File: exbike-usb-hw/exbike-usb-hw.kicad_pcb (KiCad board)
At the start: 2 copper layers, 18.3 x 51.3 mm, 18 parts, among them J1 ICSP, J2 USB_B, J3 AudioJack3_SwitchTR, U1 ATtiny24A-SS, U2 AMS1117-3.3, Y1 12 MHz

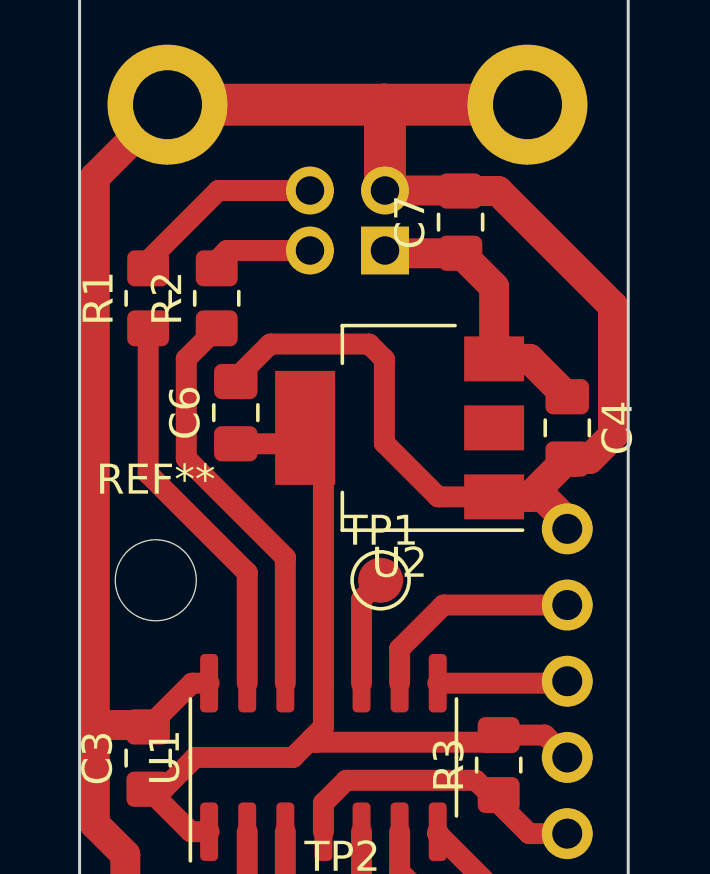
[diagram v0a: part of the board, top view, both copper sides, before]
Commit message: Add d- pullup:
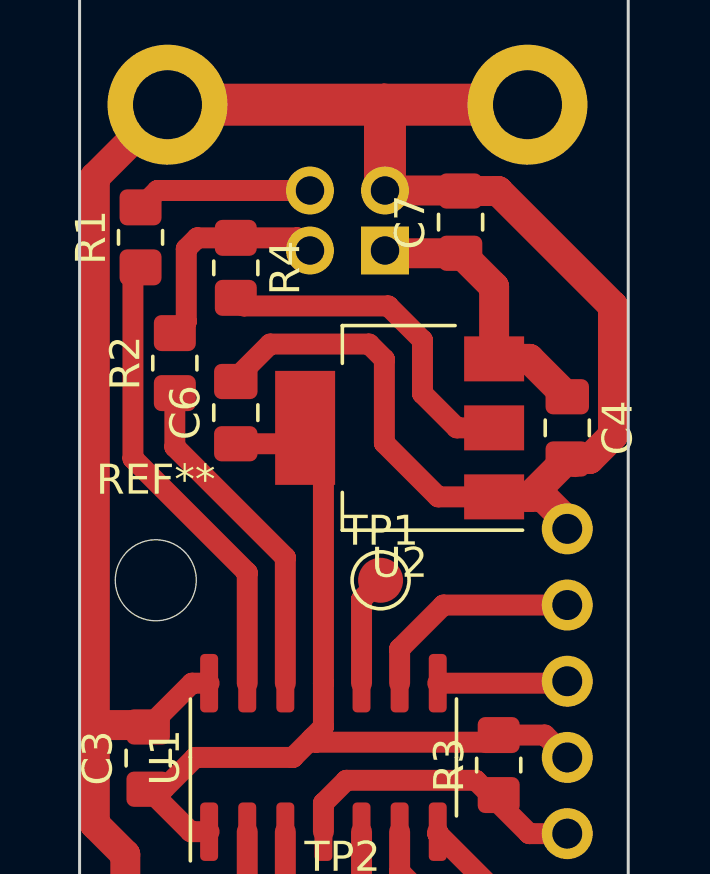
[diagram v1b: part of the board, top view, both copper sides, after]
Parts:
- added R4: 1.5k, Resistor_SMD:R_0805_2012Metric_Pad1.20x1.40mm_HandSolder, F.Cu at (66.4, 35.1)
- moved R2 2.57 mm to (64.4, 38.2)
- moved R1 2.05 mm to (63.2, 34.0)
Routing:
- net +3V3: track 31.3 -> 42.8 mm
- net D-: track 3.61 -> 7.42 mm
- net Net-(U1-PA1): track 13.6 -> 11.2 mm
- net Net-(U1-AREF/PA0): track 13.2 -> 15.5 mm
- net D+: track 6.72 -> 5.88 mm
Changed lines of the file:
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@@
+    )
+  )
+  (footprint "Resistor_SMD:R_0805_2012Metric_Pad1.20x1.40mm_HandSolder" (layer "F.Cu")
+    (at 66.421 35.052 -90)
+    (descr "Resistor SMD 0805 (2012 Metric), square (rectangular) end terminal, IPC_7351 nominal with elongated pad for handsoldering. (Body size source: IPC-SM-782 page 72, https://www.pcb-3d.com/wordpress/wp-content/uploads/ipc-sm-782a_amendment_1_and_2.pdf), generated with kicad-footprint-generator")
+    (tags "resistor handsolder")
+    (property "Sheetfile" "exbike-usb-hw.kicad_sch")
+    (property "Sheetname" "")
+    (property "ki_description" "Resistor")
+    (property "ki_keywords" "R res resistor")
+    (attr smd)
+    (fp_text reference "R4" (at 0 -1.65 90) (layer "F.SilkS")
+        (effects (font (size 1 1) (thickness 0.15)))
+    )
+    (fp_text value "1.5k" (at 0 1.65 90) (layer "F.Fab")
+        (effects (font (size 1 1) (thickness 0.15)))
+    )
+    (fp_text user "${REFERENCE}" (at 0 0 90) (layer "F.Fab")
+        (effects (font (size 0.5 0.5) (thickness 0.08)))
+    )
+    (fp_line (start -0.227064 -0.735) (end 0.227064 -0.735)
+      (stroke (width 0.12) (type solid)) (layer "F.SilkS"))
+    (fp_line (start -0.227064 0.735) (end 0.227064 0.735)
+      (stroke (width 0.12) (type solid)) (layer "F.SilkS"))
+    (fp_line (start -1.85 -0.95) (end 1.85 -0.95)
+      (stroke (width 0.05) (type solid)) (layer "F.CrtYd"))
+    (fp_line (start -1.85 0.95) (end -1.85 -0.95)
+      (stroke (width 0.05) (type solid)) (layer "F.CrtYd"))
+    (fp_line (start 1.85 -0.95) (end 1.85 0.95)
+      (stroke (width 0.05) (type solid)) (layer "F.CrtYd"))
+    (fp_line (start 1.85 0.95) (end -1.85 0.95)
+      (stroke (width 0.05) (type solid)) (layer "F.CrtYd"))
+    (fp_line (start -1 -0.625) (end 1 -0.625)
+      (stroke (width 0.1) (type solid)) (layer "F.Fab"))
+    (fp_line (start -1 0.625) (end -1 -0.625)
+      (stroke (width 0.1) (type solid)) (layer "F.Fab"))
+    (fp_line (start 1 -0.625) (end 1 0.625)
+      (stroke (width 0.1) (type solid)) (layer "F.Fab"))
+    (fp_line (start 1 0.625) (end -1 0.625)
+      (stroke (width 0.1) (type solid)) (layer "F.Fab"))
+    (pad "1" smd roundrect (at -1 0 270) (size 1.2 1.4) (layers "F.Cu" "F.Paste" "F.Mask") (roundrect_rratio 0.208333)
+      (net 10 "D-") (pintype "passive"))
+    (pad "2" smd roundrect (at 1 0 270) (size 1.2 1.4) (layers "F.Cu" "F.Paste" "F.Mask") (roundrect_rratio 0.208333)
+      (net 4 "+3V3") (pintype "passive"))
+    (model "${KICAD6_3DMODEL_DIR}/Resistor_SMD.3dshapes/R_0805_2012Metric.wrl"
+      (offset (xyz 0 0 0))
+      (scale (xyz 1 1 1))
+      (rotate (xyz 0 0 0))
     )
   )
@@
   )
   (footprint "Resistor_SMD:R_0805_2012Metric_Pad1.20x1.40mm_HandSolder" (layer "F.Cu")
-    (at 65.786 36.068 90)
+    (at 64.389 38.227 90)
     (descr "Resistor SMD 0805 (2012 Metric), square (rectangular) end terminal, IPC_7351 nominal with elongated pad for handsoldering. (Body size source: IPC-SM-782 page 72, https://www.pcb-3d.com/wordpress/wp-content/uploads/ipc-sm-782a_amendment_1_and_2.pdf), generated with kicad-footprint-generator")
     (tags "resistor handsolder")
@@
   )
   (footprint "Resistor_SMD:R_0805_2012Metric_Pad1.20x1.40mm_HandSolder" (layer "F.Cu")
-    (at 63.5 36.068 90)
+    (at 63.246 34.036 90)
     (descr "Resistor SMD 0805 (2012 Metric), square (rectangular) end terminal, IPC_7351 nominal with elongated pad for handsoldering. (Body size source: IPC-SM-782 page 72, https://www.pcb-3d.com/wordpress/wp-content/uploads/ipc-sm-782a_amendment_1_and_2.pdf), generated with kicad-footprint-generator")
     (tags "resistor handsolder")
@@
         (effects (font (size 1 1) (thickness 0.15)))
     )
-    (fp_text value "68" (at 0 1.65 90) (layer "F.Fab")
+    (fp_text value "68" (at 0 1.65 90) (layer "F.Fab") hide
         (effects (font (size 1 1) (thickness 0.15)))
     )
@@
   (segment (start 68.072 53.8465) (end 68.072 56.4515) (width 0.7) (layer "F.Cu") (net 3))
   (segment (start 68.072 56.4515) (end 69.342 57.7215) (width 0.7) (layer "F.Cu") (net 3))
+  (segment (start 71.501 36.322) (end 72.644 37.465) (width 0.7) (layer "F.Cu") (net 4))
   (segment (start 65.532 53.8465) (end 64.916 53.8465) (width 0.7) (layer "F.Cu") (net 4))
+  (segment (start 66.691 36.322) (end 71.501 36.322) (width 0.7) (layer "F.Cu") (net 4))
   (segment (start 64.008 52.4305) (end 63.5 52.4305) (width 0.7) (layer "F.Cu") (net 4))
   (segment (start 68.961 50.7365) (end 68.326 51.3715) (width 0.7) (layer "F.Cu") (net 4))
+  (segment (start 66.421 36.052) (end 66.691 36.322) (width 0.7) (layer "F.Cu") (net 4))
   (segment (start 65.067 51.3715) (end 64.008 52.4305) (width 0.7) (layer "F.Cu") (net 4))
   (segment (start 64.916 53.8465) (end 63.5 52.4305) (width 0.7) (layer "F.Cu") (net 4))
   (segment (start 68.326 51.3715) (end 65.067 51.3715) (width 0.7) (layer "F.Cu") (net 4))
   (segment (start 69.342 48.8965) (end 69.342 50.3555) (width 0.7) (layer "F.Cu") (net 4))
+  (segment (start 72.644 37.465) (end 72.644 39.243) (width 0.7) (layer "F.Cu") (net 4))
   (segment (start 66.294 40.9155) (end 68.2025 40.9155) (width 0.7) (layer "F.Cu") (net 4))
   (segment (start 69.088 50.8635) (end 68.961 50.7365) (width 0.7) (layer "F.Cu") (net 4))
+  (segment (start 72.644 39.243) (end 73.787 40.386) (width 0.7) (layer "F.Cu") (net 4))
   (segment (start 75.184 50.6255) (end 76.724 50.6255) (width 0.7) (layer "F.Cu") (net 4))
   (segment (start 69.342 40.996) (end 68.732 40.386) (width 0.7) (layer "F.Cu") (net 4))
+  (segment (start 73.787 40.386) (end 75.032 40.386) (width 0.7) (layer "F.Cu") (net 4))
   (segment (start 76.724 50.6255) (end 77.47 51.3715) (width 0.7) (layer "F.Cu") (net 4))
   (segment (start 69.342 48.8965) (end 69.342 40.996) (width 0.7) (layer "F.Cu") (net 4))
@@
   (segment (start 77.724 56.4515) (end 75.692 56.4515) (width 0.7) (layer "F.Cu") (net 9))
   (segment (start 73.152 53.9115) (end 73.152 53.8465) (width 0.7) (layer "F.Cu") (net 9))
-  (segment (start 66.1265 34.4735) (end 65.532 35.068) (width 0.7) (layer "F.Cu") (net 10))
-  (segment (start 68.894 34.4735) (end 66.1265 34.4735) (width 0.7) (layer "F.Cu") (net 10))
-  (segment (start 68.894 32.4735) (end 65.8405 32.4735) (width 0.7) (layer "F.Cu") (net 11))
-  (segment (start 65.8405 32.4735) (end 63.246 35.068) (width 0.7) (layer "F.Cu") (net 11))
+  (segment (start 68.4725 34.052) (end 68.894 34.4735) (width 0.7) (layer "F.Cu") (net 10))
+  (segment (start 65.135 34.052) (end 64.77 34.417) (width 0.7) (layer "F.Cu") (net 10))
+  (segment (start 64.77 36.846) (end 64.389 37.227) (width 0.7) (layer "F.Cu") (net 10))
+  (segment (start 66.421 34.052) (end 65.135 34.052) (width 0.7) (layer "F.Cu") (net 10))
+  (segment (start 64.77 34.417) (end 64.77 36.846) (width 0.7) (layer "F.Cu") (net 10))
+  (segment (start 66.421 34.052) (end 68.4725 34.052) (width 0.7) (layer "F.Cu") (net 10))
+  (segment (start 68.894 32.4735) (end 63.8085 32.4735) (width 0.7) (layer "F.Cu") (net 11))
+  (segment (start 63.8085 32.4735) (end 63.246 33.036) (width 0.7) (layer "F.Cu") (net 11))
   (segment (start 73.914 61.595) (end 73.914 57.2135) (width 1) (layer "F.Cu") (net 14))
   (segment (start 70.144 74.618) (end 70.144 65.365) (width 1) (layer "F.Cu") (net 14))
@@
   (segment (start 70.144 65.365) (end 73.914 61.595) (width 1) (layer "F.Cu") (net 14))
   (segment (start 71.882 55.1815) (end 73.914 57.2135) (width 0.7) (layer "F.Cu") (net 14))
-  (segment (start 66.802 48.8965) (end 66.802 45.212) (width 0.7) (layer "F.Cu") (net 16))
-  (segment (start 66.802 45.212) (end 63.5 41.91) (width 0.7) (layer "F.Cu") (net 16))
-  (segment (start 63.5 41.91) (end 63.5 37.068) (width 0.7) (layer "F.Cu") (net 16))
-  (segment (start 64.77 41.402) (end 64.77 38.084) (width 0.7) (layer "F.Cu") (net 17))
-  (segment (start 64.77 38.084) (end 65.786 37.068) (width 0.7) (layer "F.Cu") (net 17))
-  (segment (start 68.072 44.704) (end 64.77 41.402) (width 0.7) (layer "F.Cu") (net 17))
+  (segment (start 63.246 35.036) (end 62.992 35.29) (width 0.7) (layer "F.Cu") (net 16))
+  (segment (start 62.992 35.29) (end 62.992 41.402) (width 0.7) (layer "F.Cu") (net 16))
+  (segment (start 62.992 41.402) (end 66.802 45.212) (width 0.7) (layer "F.Cu") (net 16))
+  (segment (start 66.802 45.212) (end 66.802 48.8965) (width 0.7) (layer "F.Cu") (net 16))
   (segment (start 68.072 48.8965) (end 68.072 44.704) (width 0.7) (layer "F.Cu") (net 17))
+  (segment (start 64.389 41.021) (end 64.389 39.227) (width 0.7) (layer "F.Cu") (net 17))
+  (segment (start 68.072 44.704) (end 64.389 41.021) (width 0.7) (layer "F.Cu") (net 17))
   (segment (start 70.612 46.101) (end 71.247 45.466) (width 0.7) (layer "F.Cu") (net 18))
   (segment (start 70.612 48.8965) (end 70.612 46.101) (width 0.7) (layer "F.Cu") (net 18))

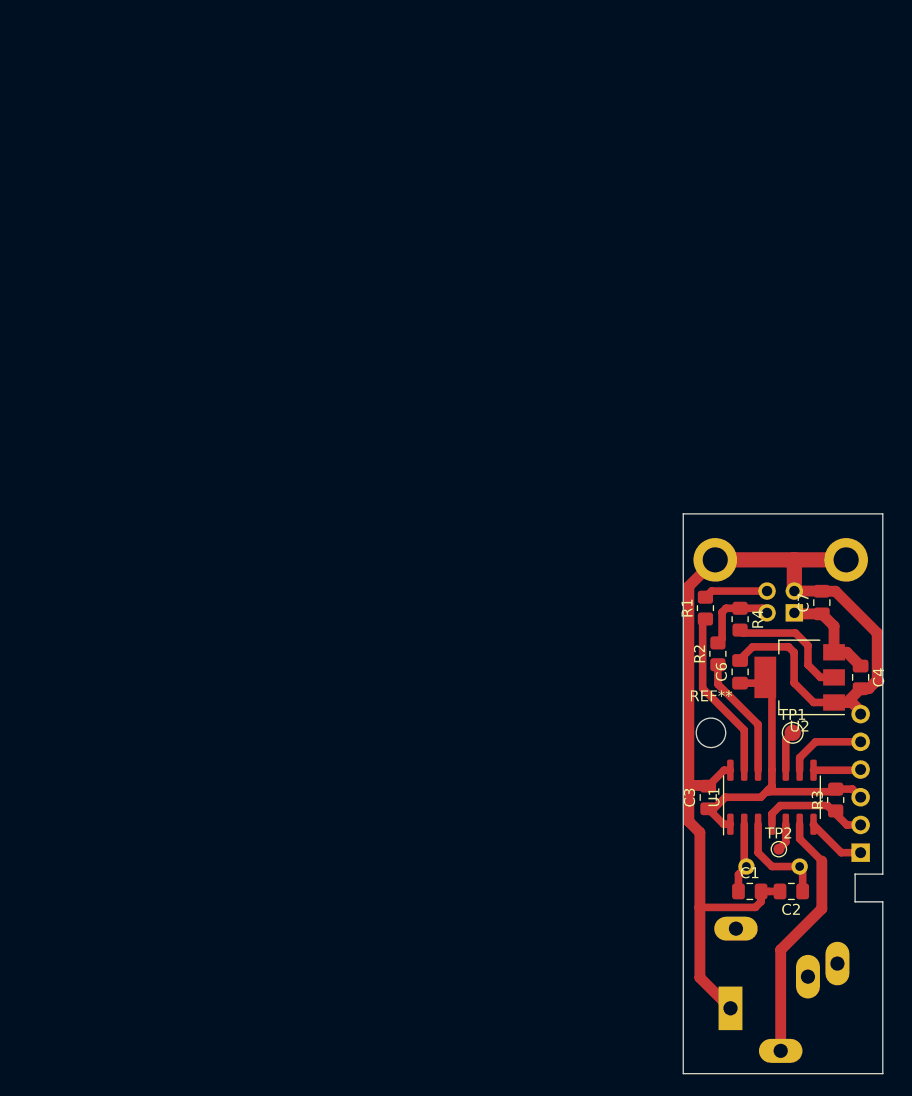
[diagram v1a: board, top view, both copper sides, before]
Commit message: Early USB code, PCB project cleanup
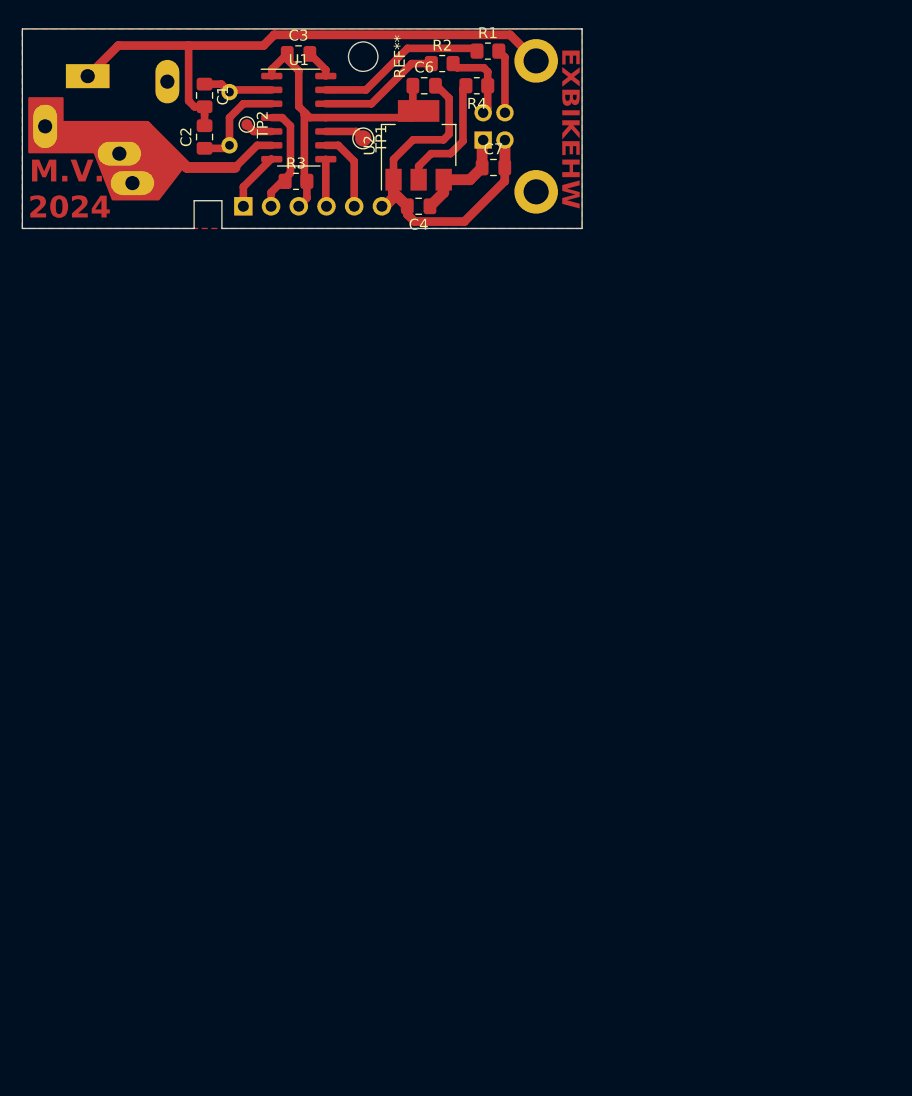
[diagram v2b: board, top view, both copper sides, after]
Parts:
- moved J3 103.8 mm to (6.62, -14.7), turned to 0 degrees
- moved C1 88.4 mm to (17.3, -13.0), turned to -90 degrees
- moved C2 87.6 mm to (17.3, -9.14), turned to 90 degrees
- moved Y1 84.3 mm to (19.6, -8.38), turned to 90 degrees
- moved TP2 82.4 mm to (21.2, -10.3), turned to -90 degrees
- moved J1 81.9 mm to (20.9, -2.79), turned to -90 degrees
- moved C3 77.8 mm to (25.9, -16.8), turned to 0 degrees
- moved U1 75.9 mm to (26.0, -10.9), turned to 0 degrees
- moved R3 75.2 mm to (25.7, -5.08), turned to 0 degrees
- moved REF** 69.7 mm to (31.9, -16.5), turned to -90 degrees
- moved TP1 67.2 mm to (31.9, -9.02), turned to -90 degrees
- moved C6 61.0 mm to (37.5, -13.8), turned to 0 degrees
- moved U2 60.0 mm to (37.0, -8.38), turned to 90 degrees
- moved R2 59.7 mm to (39.1, -15.9), turned to 0 degrees
- moved C4 59.2 mm to (37.0, -2.79), turned to 180 degrees
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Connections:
- J3 pad R: unconnected-(J3-PadR) -> SW_IN
- J3 pad RN: unconnected-(J3-PadRN) -> SW_IN
- J3 pad TN: unconnected-(J3-PadTN) -> GND
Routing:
- net GND: track 105.8 -> 89.0 mm
- net SW_IN: track 23.2 -> 28.9 mm
- added copper zone on F.Cu, net GND
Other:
- board size 18.3 x 51.3 mm -> 51.3 x 18.3 mm
- board text added: "2024"
- board text added: "EXBIKEHW"
- board text added: "M.V."
